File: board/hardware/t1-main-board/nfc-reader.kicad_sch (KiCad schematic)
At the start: 34 parts, among them U5801 PN7160A1HN-C100E, U5802 TPS22919DCKR, Y5801 27.12 MHz

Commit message: Board on libs v0.2.0: lower-case kebab vendor keys (HL-13)
The libs submodule moves to v0.2.0 (5f24483). Every library nickname in
the generator, the placement tool and the floorplan study follows the
key table (Texas_Instruments -> texas-instruments, OpenDAP_Device ->
opendap-generic, Rockchip and Rockchip_PMIC -> rockchip, ...); the
library tables are written from the files. Schematic and board
regenerated.

Checks: ERC 0 errors (warnings unchanged); DRC 0 errors, 605 warnings,
the same counts by type, schematic parity 0; every placement identical;
craft Q1 met; pcb tests pass; STEP export resolves every libs 3D model
(the 27 parts without a model are KiCad stock lands that have none).

Co-Authored-By: Claude Opus 5.5 <noreply@anthropic.com>
Claude-Session: https://claude.ai/code/session_01Ei262h3TpgY9vyfNLMi5Mn
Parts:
- U5801: footprint NXP:NXP_SOT618-1_HVQFN-40-1EP_6x6mm_P0.5mm_EP4.1x4.1mm -> nxp:NXP_SOT618-1_HVQFN-40-1EP_6x6mm_P0.5mm_EP4.1x4.1mm; symbol NXP:PN7160A1HN-C100E -> nxp:PN7160A1HN-C100E
- U5802: footprint Texas_Instruments:Texas_DCK0006A_SC-70-6_1.25x2mm_P0.65mm -> texas-instruments:Texas_DCK0006A_SC-70-6_1.25x2mm_P0.65mm; symbol Texas_Instruments:TPS22919DCKR -> texas-instruments:TPS22919DCKR
- Y5801: symbol OpenDAP_Device:Crystal_GND24 -> opendap-generic:Crystal_GND24
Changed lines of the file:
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@@
 (paper "A3")
 (title_block (title "NFC controller") (date "2026-10-25") (rev "A") (company "The OpenDAP Project") (comment 1 "blk.nfc-reader") (comment 2 "PN7160 on I2C2 at 0x28: NFC_VBAT switch, EMC filter, matching, RX path and 27.12 MHz crystal"))
-(symbol (lib_id "NXP:PN7160A1HN-C100E") (at 71.12 109.22 0) (unit 1) (body_style 1) (exclude_from_sim no) (in_bom yes) (on_board yes) (dnp no)
+(symbol (lib_id "nxp:PN7160A1HN-C100E") (at 71.12 109.22 0) (unit 1) (body_style 1) (exclude_from_sim no) (in_bom yes) (on_board yes) (dnp no)
   (property "Reference" "U5801" (at 85.09 67.31 0) (effects (font (size 1.27 1.27)) (justify left)))
   (property "Value" "PN7160A1HN-C100E" (at 85.09 64.77 0) (effects (font (size 1.27 1.27)) (justify left)))
-  (property "Footprint" "NXP:NXP_SOT618-1_HVQFN-40-1EP_6x6mm_P0.5mm_EP4.1x4.1mm" (at 71.12 109.22 0) (effects (font (size 1.27 1.27))) (hide yes))
+  (property "Footprint" "nxp:NXP_SOT618-1_HVQFN-40-1EP_6x6mm_P0.5mm_EP4.1x4.1mm" (at 71.12 109.22 0) (effects (font (size 1.27 1.27))) (hide yes))
   (property "Datasheet" "https://www.nxp.com/docs/en/data-sheet/PN7160_PN7161.pdf" (at 71.12 109.22 0) (effects (font (size 1.27 1.27))) (hide yes))
   (property "Description" "PN7160 NFC controller, NCI, integrated firmware, I2C host interface, reader/writer, card emulation, P2P, HVQFN40 (SOT618-1) 6 x 6 mm, exposed pad" (at 71.12 109.22 0) (effects (font (size 1.27 1.27))) (hide yes))
@@
 (rectangle (start 22.86 35.56) (end 190.5 163.83) (stroke (width 0) (type dash)) (fill (type none)))
 (text "PN7160 at I2C2 0x28 (BOM v1 line 127; AN12988 Table 9)" (exclude_from_sim no) (at 24.13 34.29 0) (effects (font (size 2.54 2.54)) (justify left bottom)))
-(symbol (lib_id "OpenDAP_Device:Crystal_GND24") (at 219.71 48.26 0) (unit 1) (body_style 1) (exclude_from_sim no) (in_bom yes) (on_board yes) (dnp no)
+(symbol (lib_id "opendap-generic:Crystal_GND24") (at 219.71 48.26 0) (unit 1) (body_style 1) (exclude_from_sim no) (in_bom yes) (on_board yes) (dnp no)
   (property "Reference" "Y5801" (at 223.52 43.18 0) (effects (font (size 1.27 1.27)) (justify left)))
   (property "Value" "27.12 MHz" (at 223.52 54.61 0) (effects (font (size 1.27 1.27)) (justify left)))
@@
 (rectangle (start 195.58 35.56) (end 308.61 71.12) (stroke (width 0) (type dash)) (fill (type none)))
 (text "27.12 MHz crystal (DS Table 17; AN14518 Table 9)" (exclude_from_sim no) (at 196.85 34.29 0) (effects (font (size 2.54 2.54)) (justify left bottom)))
-(symbol (lib_id "Texas_Instruments:TPS22919DCKR") (at 223.52 104.14 0) (unit 1) (body_style 1) (exclude_from_sim no) (in_bom yes) (on_board yes) (dnp no)
+(symbol (lib_id "texas-instruments:TPS22919DCKR") (at 223.52 104.14 0) (unit 1) (body_style 1) (exclude_from_sim no) (in_bom yes) (on_board yes) (dnp no)
   (property "Reference" "U5802" (at 215.9 88.9 0) (effects (font (size 1.27 1.27)) (justify left)))
   (property "Value" "TPS22919DCKR" (at 215.9 86.36 0) (effects (font (size 1.27 1.27)) (justify left)))
-  (property "Footprint" "Texas_Instruments:Texas_DCK0006A_SC-70-6_1.25x2mm_P0.65mm" (at 223.52 104.14 0) (effects (font (size 1.27 1.27))) (hide yes))
+  (property "Footprint" "texas-instruments:Texas_DCK0006A_SC-70-6_1.25x2mm_P0.65mm" (at 223.52 104.14 0) (effects (font (size 1.27 1.27))) (hide yes))
   (property "Datasheet" "https://www.ti.com/lit/ds/symlink/tps22919.pdf" (at 223.52 104.14 0) (effects (font (size 1.27 1.27))) (hide yes))
   (property "Description" "Load switch, 1.6-5.5 V, 1.5 A, 90 mOhm, controlled rise time, short-circuit protection, adjustable quick output discharge, SOT/SC-70-6 (DCK0006A)" (at 223.52 104.14 0) (effects (font (size 1.27 1.27))) (hide yes))

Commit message: Board in the 62.5 x 95.0 mm body: ADR 0025, outline 59.1 x 91.6, 0201 swaps
ADR 0025 supersedes ADR 0016 for t1 ADR 0006's body: board outline from
the body, 1.2 mm walls and 0.5 mm clearance; height zones and stack
restated unchanged; the speaker on a case shelf (PCB-Z-09); pocket
reliefs at the 4.4 mm jack, the microSD (DM3AT push-push kept) and the
side buttons; the audio 0603 -> 0402 swap gated by t1 V2-A08; reserve
(NFC reader, then TPM) recorded, not applied.

- pcb/geometry.py derives the outline from BODY, WALL and CLEARANCE;
  the pocket, display and fixed parts keep their device-frame positions;
  holes keep their edge distance; the speaker shadow becomes a 1.5 mm
  shelf height area (placement, checks, occupancy).
- build.py reports pocket reliefs and routing room; C904 unfixed (it
  now finds back room, so PCB-Z-04 carries no part).
- Generator: parts.area_swap puts 121 generic 0402 resistors (outside
  audio and VBUS paths, >= 10 ohm) and five 100 nF signal capacitors in
  0201 (BOM v1.16); schematic and board regenerated.
- Result: 1,012/1,012 placed, 98.8 % by the floorplan method (was 111 %),
  factor left 1.68 (was 1.49); DRC 0 errors, ERC 0 errors, 0 check
  findings, pcb tests 20/20, schematic craft Q1 met.
- Specs: PCB constraints v0.17 (M-01, M-02, M-08, Z-02, Z-06 to Z-09,
  R-07), placement v1.1 (section 3, decisions 4 and 13, checks, open
  items with the gated swaps and the reserve), floorplan v1 section 1,
  BOM v1.16.

Co-Authored-By: Claude Opus 5.5 <noreply@anthropic.com>
Claude-Session: https://claude.ai/code/session_01Ei262h3TpgY9vyfNLMi5Mn
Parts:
- R5804, R5805: footprint Resistor_SMD:R_0402_1005Metric -> Resistor_SMD:R_0201_0603Metric; MPN RC0402FR-072K2L -> RC0201FR-072K2L
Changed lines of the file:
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@@
   (property "Reference" "R5804" (at 320.04 90.17 0) (effects (font (size 1.27 1.27)) (justify left)))
   (property "Value" "2.2 kΩ" (at 320.04 92.71 0) (effects (font (size 1.27 1.27)) (justify left)))
-  (property "Footprint" "Resistor_SMD:R_0402_1005Metric" (at 318.77 91.44 0) (effects (font (size 1.27 1.27))) (hide yes))
-  (property "Datasheet" "https://yageogroup.com/en/ProductSearch/PartNumberSearch?part=RC0402FR-072K2L" (at 318.77 91.44 0) (effects (font (size 1.27 1.27))) (hide yes))
-  (property "Description" "Resistor, 2.2 kΩ, 1 %, 1/16 W, 0402" (at 318.77 91.44 0) (effects (font (size 1.27 1.27))) (hide yes))
+  (property "Footprint" "Resistor_SMD:R_0201_0603Metric" (at 318.77 91.44 0) (effects (font (size 1.27 1.27))) (hide yes))
+  (property "Datasheet" "https://yageogroup.com/en/ProductSearch/PartNumberSearch?part=RC0201FR-072K2L" (at 318.77 91.44 0) (effects (font (size 1.27 1.27))) (hide yes))
+  (property "Description" "Resistor, 2.2 kΩ, 1 %, 1/20 W, 0201" (at 318.77 91.44 0) (effects (font (size 1.27 1.27))) (hide yes))
   (property "Manufacturer" "YAGEO" (at 318.77 91.44 0) (effects (font (size 1.27 1.27))) (hide yes))
-  (property "MPN" "RC0402FR-072K2L" (at 318.77 91.44 0) (effects (font (size 1.27 1.27))) (hide yes))
+  (property "MPN" "RC0201FR-072K2L" (at 318.77 91.44 0) (effects (font (size 1.27 1.27))) (hide yes))
   (property "Block" "blk.nfc-reader" (at 318.77 91.44 0) (effects (font (size 1.27 1.27))) (hide yes))
   (pin "1")
@@
   (property "Reference" "R5805" (at 349.25 90.17 0) (effects (font (size 1.27 1.27)) (justify left)))
   (property "Value" "2.2 kΩ" (at 349.25 92.71 0) (effects (font (size 1.27 1.27)) (justify left)))
-  (property "Footprint" "Resistor_SMD:R_0402_1005Metric" (at 347.98 91.44 0) (effects (font (size 1.27 1.27))) (hide yes))
-  (property "Datasheet" "https://yageogroup.com/en/ProductSearch/PartNumberSearch?part=RC0402FR-072K2L" (at 347.98 91.44 0) (effects (font (size 1.27 1.27))) (hide yes))
-  (property "Description" "Resistor, 2.2 kΩ, 1 %, 1/16 W, 0402" (at 347.98 91.44 0) (effects (font (size 1.27 1.27))) (hide yes))
+  (property "Footprint" "Resistor_SMD:R_0201_0603Metric" (at 347.98 91.44 0) (effects (font (size 1.27 1.27))) (hide yes))
+  (property "Datasheet" "https://yageogroup.com/en/ProductSearch/PartNumberSearch?part=RC0201FR-072K2L" (at 347.98 91.44 0) (effects (font (size 1.27 1.27))) (hide yes))
+  (property "Description" "Resistor, 2.2 kΩ, 1 %, 1/20 W, 0201" (at 347.98 91.44 0) (effects (font (size 1.27 1.27))) (hide yes))
   (property "Manufacturer" "YAGEO" (at 347.98 91.44 0) (effects (font (size 1.27 1.27))) (hide yes))
-  (property "MPN" "RC0402FR-072K2L" (at 347.98 91.44 0) (effects (font (size 1.27 1.27))) (hide yes))
+  (property "MPN" "RC0201FR-072K2L" (at 347.98 91.44 0) (effects (font (size 1.27 1.27))) (hide yes))
   (property "Block" "blk.nfc-reader" (at 347.98 91.44 0) (effects (font (size 1.27 1.27))) (hide yes))
   (pin "1")

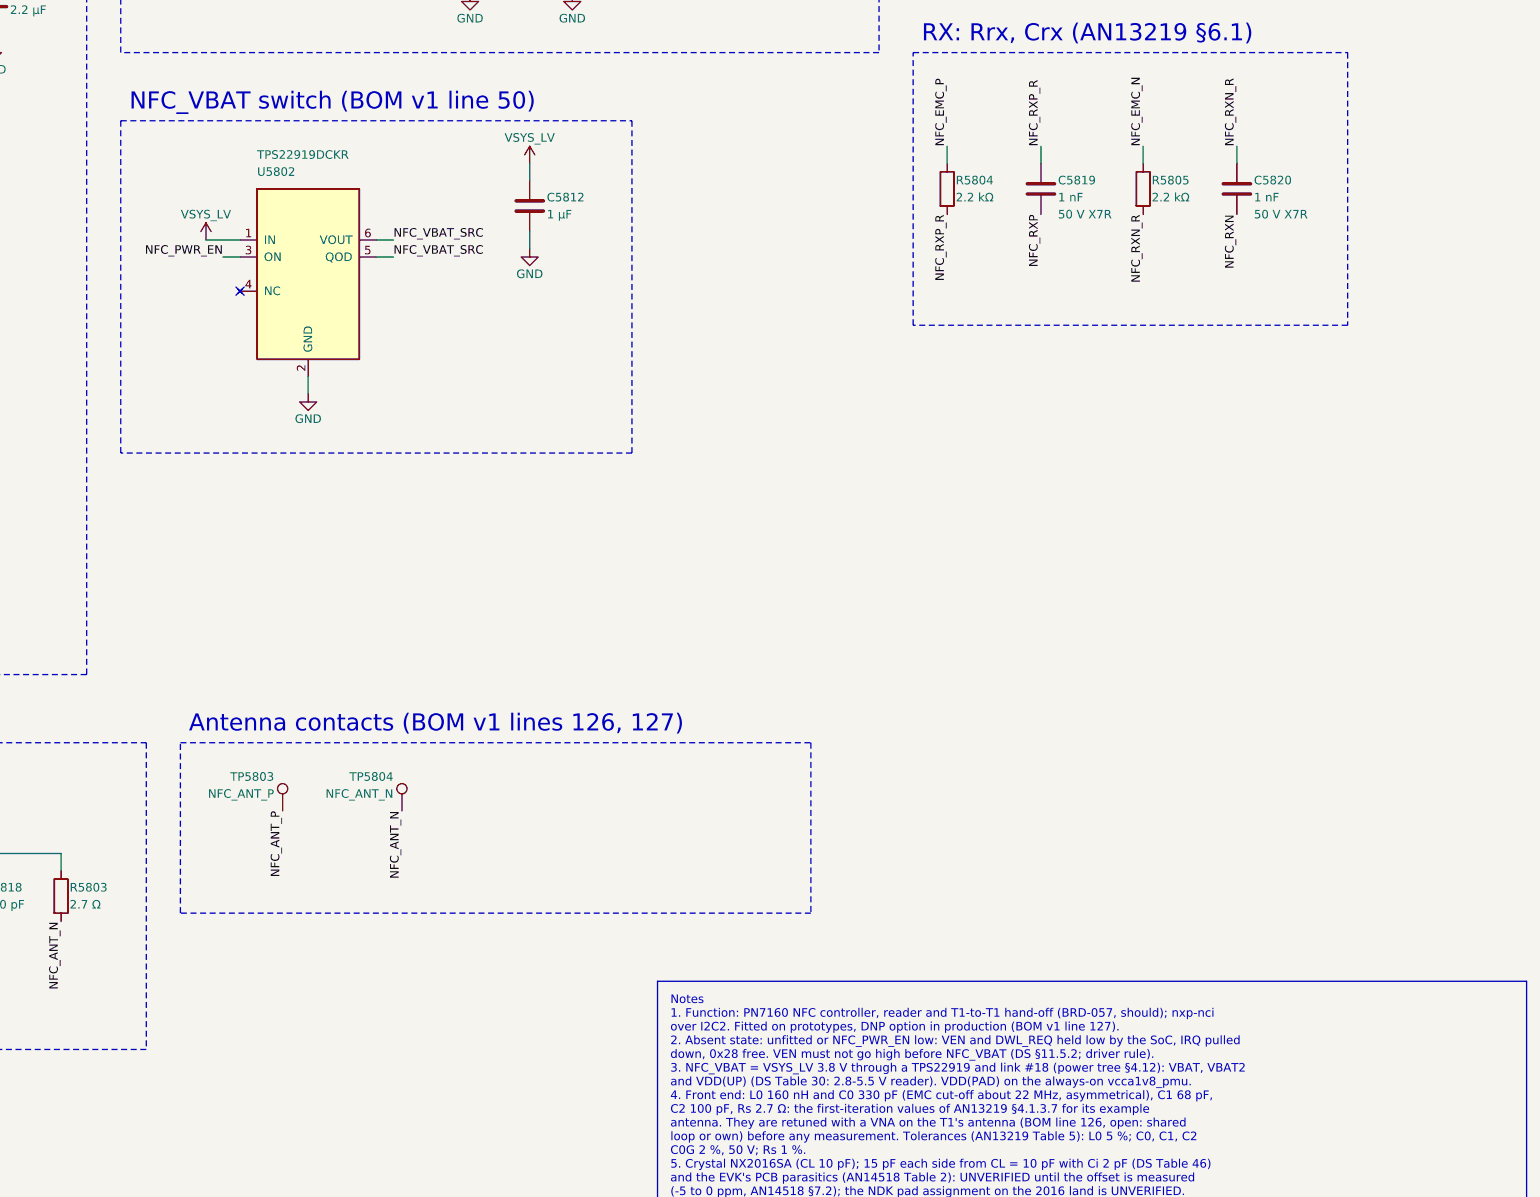
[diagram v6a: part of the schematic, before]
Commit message: Load switches in TPS22916C WCSP (BOM v1.17 item 3, libs v0.3.1)
The six TPS22919DCKR become the TPS22916CYFPR, the BOM's named second
source, now that kicad-lib v0.3.1 carries its land, symbol and model.
Each position's rise time and output discharge checked against the
data sheet (SLVSDO5F section 6.6): every sequencing rule holds; the
fixed 150 Ohm discharge is slower and the driver's delays follow it.
Power tree v0.9 restates the switch rows.

Co-Authored-By: Claude Opus 5.5 <noreply@anthropic.com>
Claude-Session: https://claude.ai/code/session_01Ei262h3TpgY9vyfNLMi5Mn
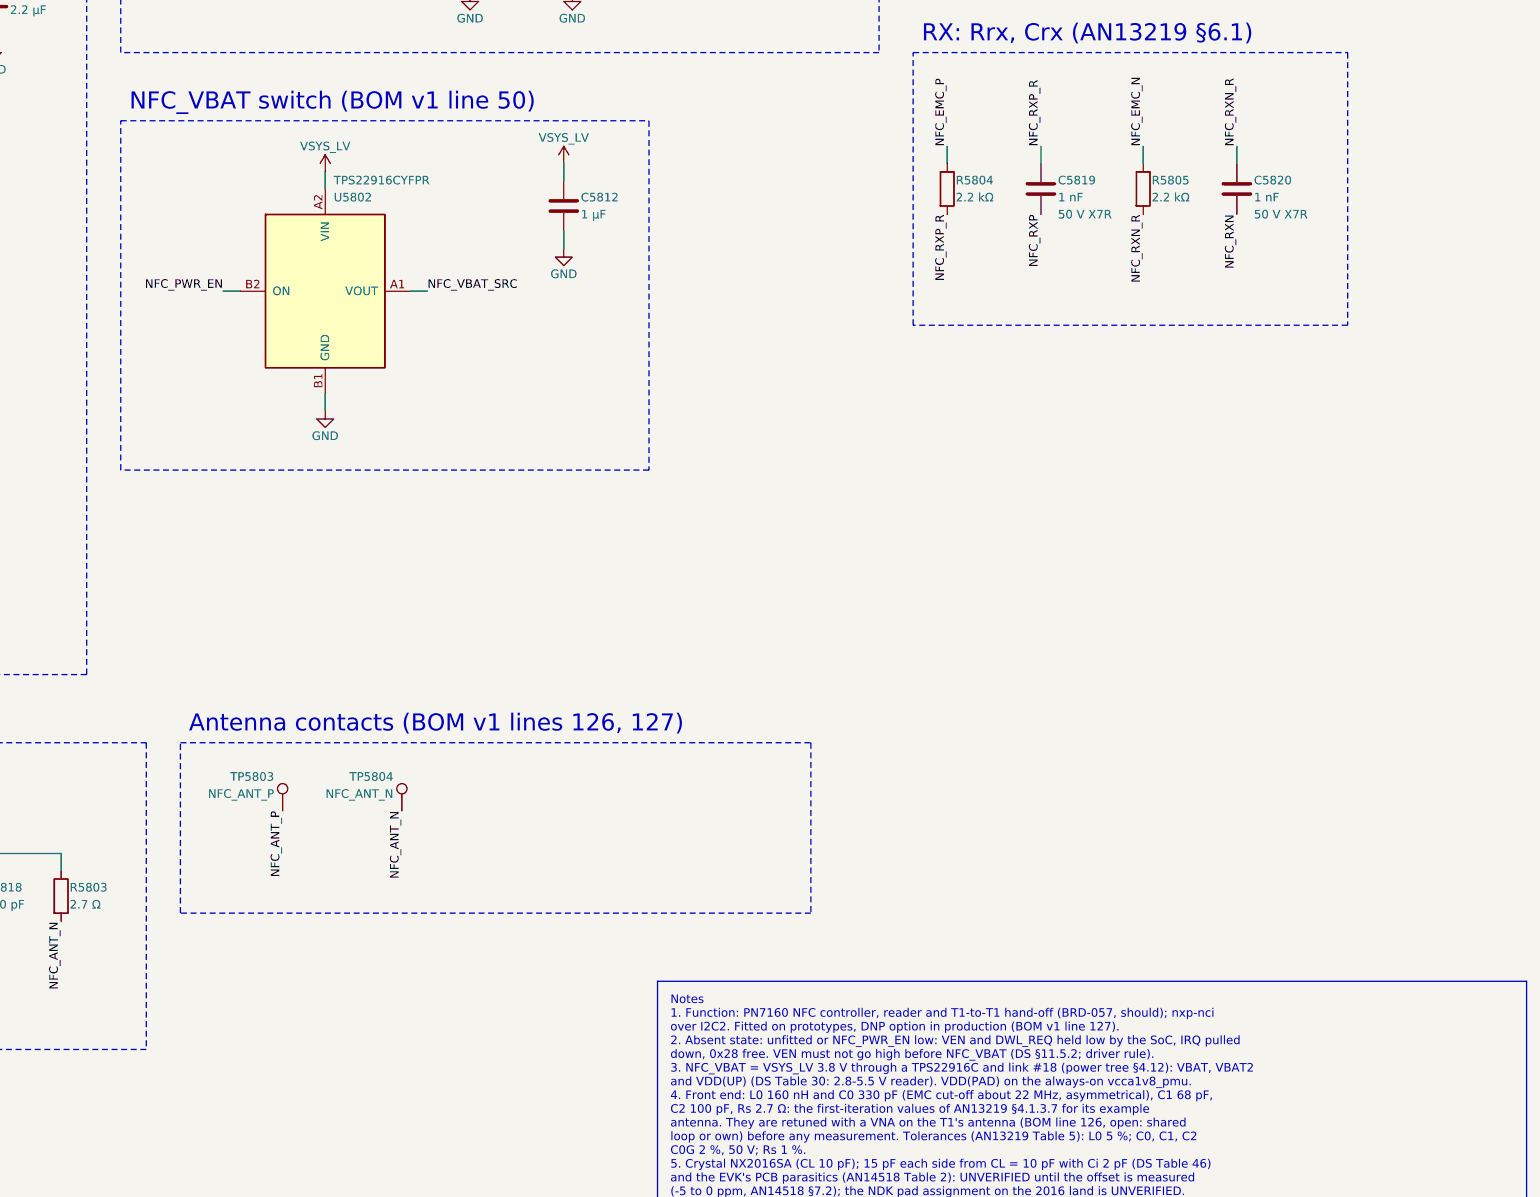
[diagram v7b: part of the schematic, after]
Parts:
- U5802: value TPS22919DCKR -> TPS22916CYFPR; footprint texas-instruments:Texas_DCK0006A_SC-70-6_1.25x2mm_P0.65mm -> texas-instruments:Texas_YFP0004_DSBGA-4_0.78x0.78mm_Layout2x2_P0.4mm; symbol texas-instruments:TPS22919DCKR -> texas-instruments:TPS22916CYFPR; MPN TPS22919DCKR -> TPS22916CYFPR; Second_Source Texas Instruments TPS22916CYFPR (WCSP, other land; BOM v1 l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 -> (none)
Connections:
- net GND: now also U5802.B1 (GND); no longer U5802.2 (GND)
- net NFC_PWR_EN: now also U5802.B2 (ON); no longer U5802.3 (ON)
- net NFC_VBAT_SRC: now also U5802.A1 (VOUT); no longer U5802.5 (QOD), U5802.6 (VOUT)
- net VSYS_LV: now also U5802.A2 (VIN); no longer U5802.1 (IN)
- no-connect marks 13 -> 12
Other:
- moved on the sheet: C5812

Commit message: BOM v1.18 item 2: successors of the discontinued 1 uF 0402
GRM155R61A105KE15D is to be discontinued. 44 positions take
GRM155C71A105KE11D (1 uF 10 V X7S); the eight TPS7A20 positions take
GRM155R61C225KE11D (2.2 uF 16 V X5R) to keep the 0.47 uF effective
minimum with 10 % to spare at up to 3.8 V. Same land; sourcing pass.
Closes BOM §7 item 52; new item 55 lists the other capture parts outside
Murata's product data or near end of life.

Co-Authored-By: Claude Opus 5.5 <noreply@anthropic.com>
Claude-Session: https://claude.ai/code/session_01Ei262h3TpgY9vyfNLMi5Mn
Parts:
- C5808, C5812: MPN GRM155R61A105KE15D -> GRM155C71A105KE11D
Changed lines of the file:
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@@
   (property "Value" "1 µF" (at 153.67 96.52 0) (effects (font (size 1.27 1.27)) (justify left)))
   (property "Footprint" "Capacitor_SMD:C_0402_1005Metric" (at 151.13 95.25 0) (effects (font (size 1.27 1.27))) (hide yes))
-  (property "Datasheet" "https://www.murata.com/en-us/products/productdetail?partno=GRM155R61A105KE15D" (at 151.13 95.25 0) (effects (font (size 1.27 1.27))) (hide yes))
-  (property "Description" "Capacitor, 1 µF, 10 V, X5R, 0402" (at 151.13 95.25 0) (effects (font (size 1.27 1.27))) (hide yes))
+  (property "Datasheet" "https://www.murata.com/en-us/products/productdetail?partno=GRM155C71A105KE11D" (at 151.13 95.25 0) (effects (font (size 1.27 1.27))) (hide yes))
+  (property "Description" "Capacitor, 1 µF, 10 V, X7S, 0402" (at 151.13 95.25 0) (effects (font (size 1.27 1.27))) (hide yes))
   (property "Manufacturer" "Murata" (at 151.13 95.25 0) (effects (font (size 1.27 1.27))) (hide yes))
-  (property "MPN" "GRM155R61A105KE15D" (at 151.13 95.25 0) (effects (font (size 1.27 1.27))) (hide yes))
+  (property "MPN" "GRM155C71A105KE11D" (at 151.13 95.25 0) (effects (font (size 1.27 1.27))) (hide yes))
   (property "Block" "blk.nfc-reader" (at 151.13 95.25 0) (effects (font (size 1.27 1.27))) (hide yes))
   (pin "1")
@@
   (property "Value" "1 µF" (at 264.16 95.25 0) (effects (font (size 1.27 1.27)) (justify left)))
   (property "Footprint" "Capacitor_SMD:C_0402_1005Metric" (at 261.62 93.98 0) (effects (font (size 1.27 1.27))) (hide yes))
-  (property "Datasheet" "https://www.murata.com/en-us/products/productdetail?partno=GRM155R61A105KE15D" (at 261.62 93.98 0) (effects (font (size 1.27 1.27))) (hide yes))
-  (property "Description" "Capacitor, 1 µF, 10 V, X5R, 0402" (at 261.62 93.98 0) (effects (font (size 1.27 1.27))) (hide yes))
+  (property "Datasheet" "https://www.murata.com/en-us/products/productdetail?partno=GRM155C71A105KE11D" (at 261.62 93.98 0) (effects (font (size 1.27 1.27))) (hide yes))
+  (property "Description" "Capacitor, 1 µF, 10 V, X7S, 0402" (at 261.62 93.98 0) (effects (font (size 1.27 1.27))) (hide yes))
   (property "Manufacturer" "Murata" (at 261.62 93.98 0) (effects (font (size 1.27 1.27))) (hide yes))
-  (property "MPN" "GRM155R61A105KE15D" (at 261.62 93.98 0) (effects (font (size 1.27 1.27))) (hide yes))
+  (property "MPN" "GRM155C71A105KE11D" (at 261.62 93.98 0) (effects (font (size 1.27 1.27))) (hide yes))
   (property "Block" "blk.nfc-reader" (at 261.62 93.98 0) (effects (font (size 1.27 1.27))) (hide yes))
   (pin "1")
